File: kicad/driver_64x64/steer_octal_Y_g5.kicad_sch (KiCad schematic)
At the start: 66 parts

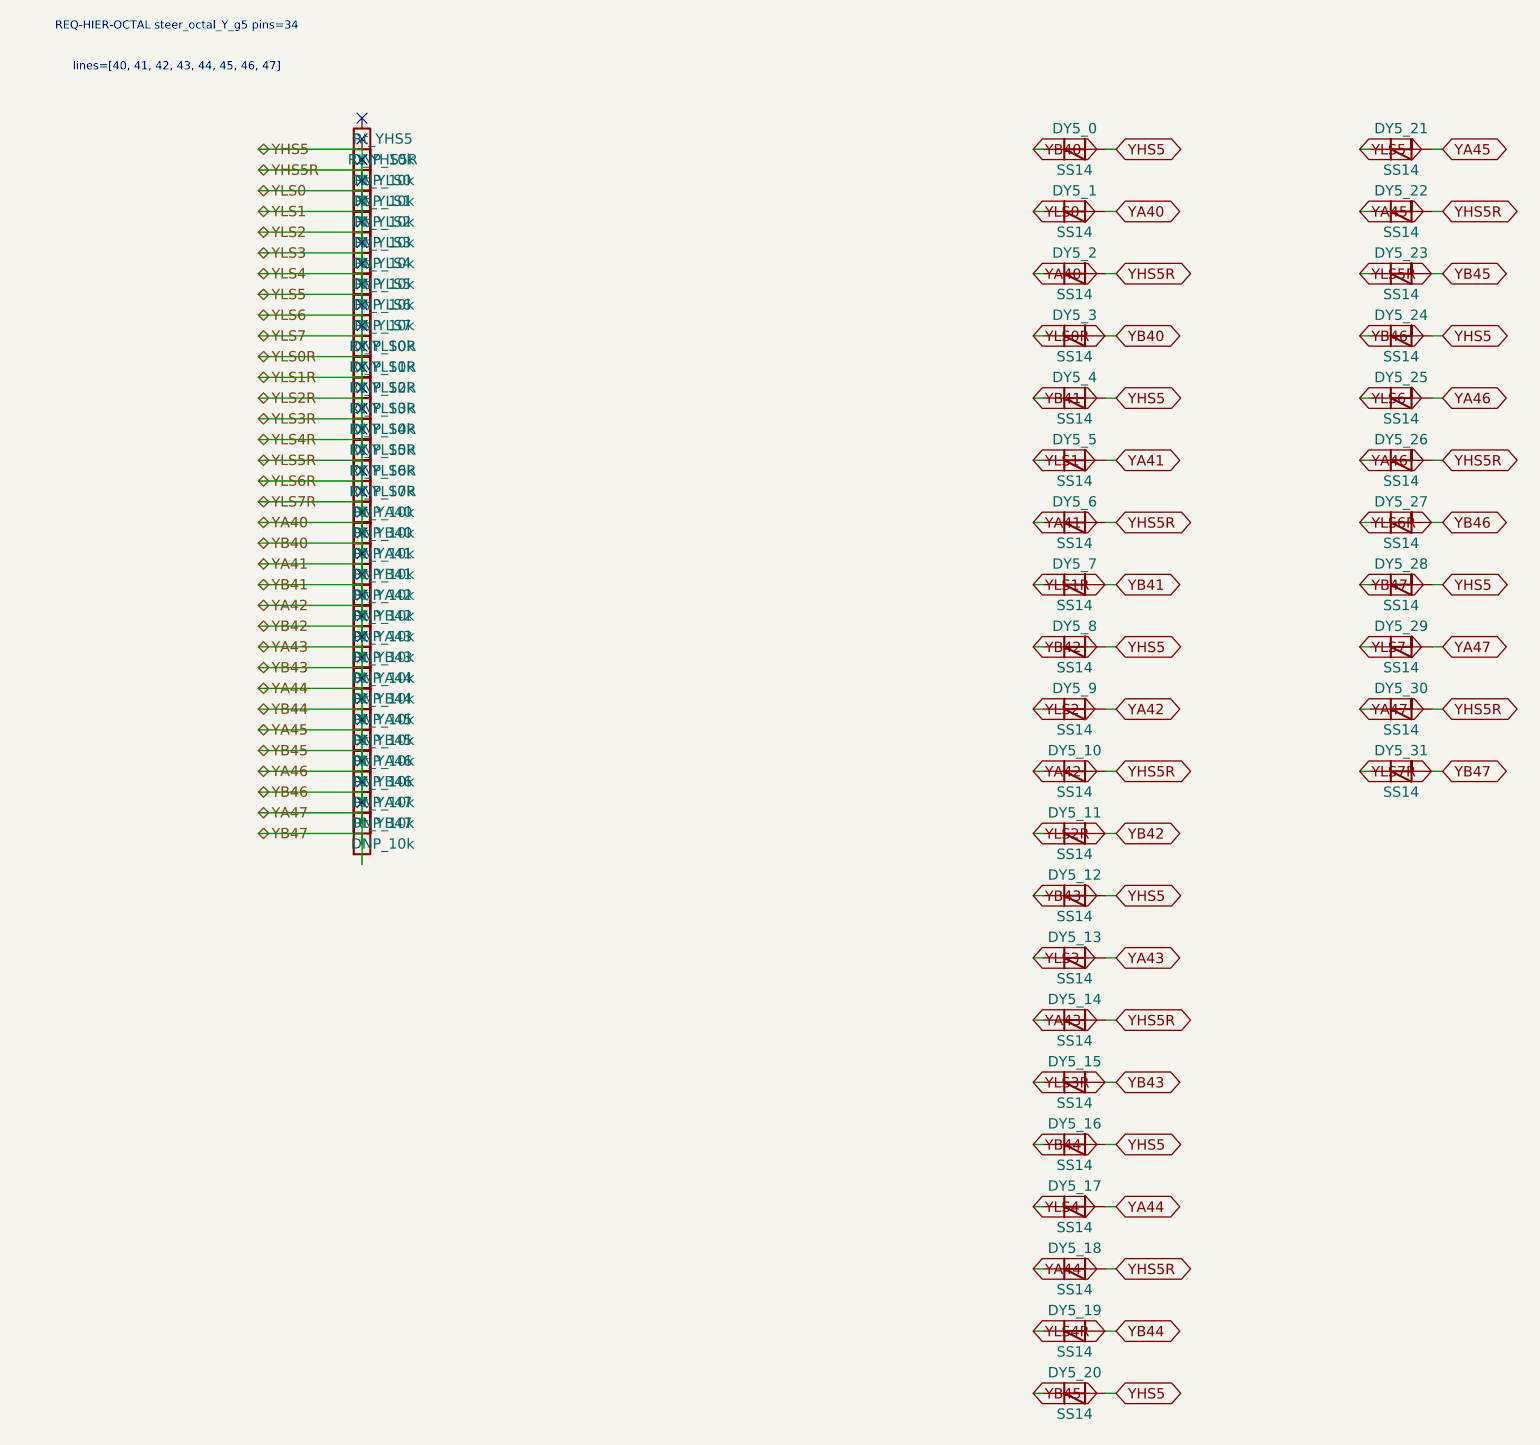
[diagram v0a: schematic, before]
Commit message: logical seperation into host and multiple decode/drive/steering boards
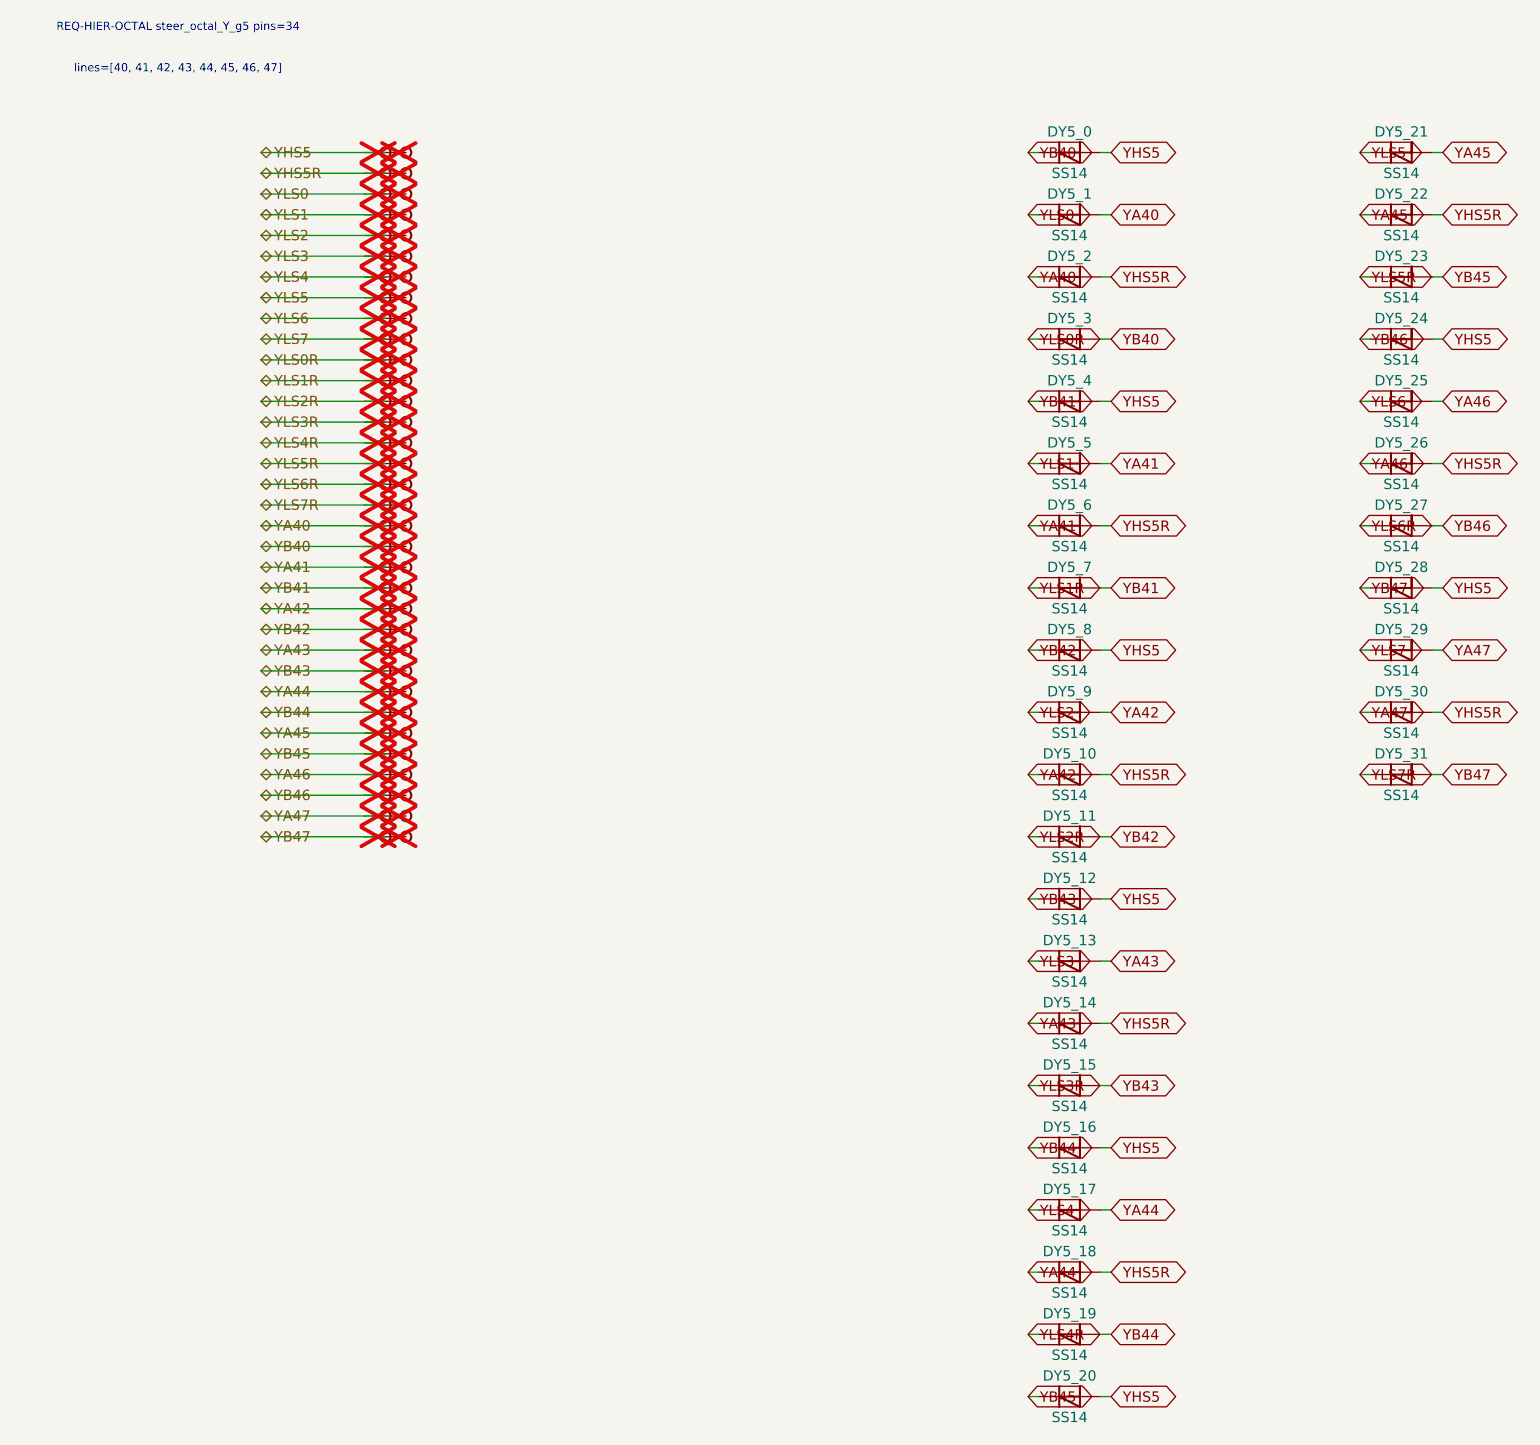
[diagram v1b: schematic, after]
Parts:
- removed Rt_YA40, Rt_YA41, Rt_YA42, Rt_YA43, Rt_YA44, Rt_YA45, Rt_YA46, Rt_YA47, Rt_YB40, Rt_YB41, Rt_YB42, Rt_YB43, Rt_YB44, Rt_YB45, Rt_YB46, Rt_YB47, Rt_YHS5, Rt_YHS5R, Rt_YLS0, Rt_YLS0R, Rt_YLS1, Rt_YLS1R, Rt_YLS2, Rt_YLS2R, Rt_YLS3, Rt_YLS3R, Rt_YLS4, Rt_YLS4R, Rt_YLS5, Rt_YLS5R, Rt_YLS6, Rt_YLS6R, Rt_YLS7, Rt_YLS7R: DNP_10k, symbol Device:R
- added TP_YA40, TP_YA40b, TP_YA41, TP_YA41b, TP_YA42, TP_YA42b, TP_YA43, TP_YA43b, TP_YA44, TP_YA44b, TP_YA45, TP_YA45b, TP_YA46, TP_YA46b, TP_YA47, TP_YA47b, TP_YB40, TP_YB40b, TP_YB41, TP_YB41b, TP_YB42, TP_YB42b, TP_YB43, TP_YB43b, TP_YB44, TP_YB44b, TP_YB45, TP_YB45b, TP_YB46, TP_YB46b, TP_YB47, TP_YB47b, TP_YHS5, TP_YHS5R, TP_YHS5Rb, TP_YHS5b, TP_YLS0, TP_YLS0R, TP_YLS0Rb, TP_YLS0b, TP_YLS1, TP_YLS1R, TP_YLS1Rb, TP_YLS1b, TP_YLS2, TP_YLS2R, TP_YLS2Rb, TP_YLS2b, TP_YLS3, TP_YLS3R, TP_YLS3Rb, TP_YLS3b, TP_YLS4, TP_YLS4R, TP_YLS4Rb, TP_YLS4b, TP_YLS5, TP_YLS5R, TP_YLS5Rb, TP_YLS5b, TP_YLS6, TP_YLS6R, TP_YLS6Rb, TP_YLS6b, TP_YLS7, TP_YLS7R, TP_YLS7Rb, TP_YLS7b: Stub, symbol CMR:Stub
- DY5_0, DY5_1, DY5_10, DY5_11, DY5_12, DY5_13, DY5_14, DY5_15, DY5_16, DY5_17, DY5_18, DY5_19, DY5_2, DY5_20, DY5_21, DY5_22, DY5_23, DY5_24, DY5_25, DY5_26, DY5_27, DY5_28, DY5_29, DY5_3, DY5_30, DY5_31, DY5_4, DY5_5, DY5_6, DY5_7, DY5_8, DY5_9: symbol Device:D_Schottky -> CMR:D_Schottky
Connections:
- net YA40: now also TP_YA40.1, TP_YA40b.1; no longer DY5_0.1 (K), DY5_0.2 (A), DY5_1.1 (K), DY5_10.1 (K), DY5_10.2 (A), DY5_11.1 (K), DY5_11.2 (A), DY5_12.1 (K), DY5_12.2 (A), DY5_13.1 (K), DY5_13.2 (A), DY5_14.1 (K), DY5_14.2 (A), DY5_15.1 (K), DY5_15.2 (A), DY5_16.1 (K), DY5_16.2 (A), DY5_17.1 (K), DY5_17.2 (A), DY5_18.1 (K), DY5_18.2 (A), DY5_19.1 (K), DY5_19.2 (A), DY5_2.2 (A), DY5_20.1 (K), DY5_20.2 (A), DY5_21.1 (K), DY5_21.2 (A), DY5_22.1 (K), DY5_22.2 (A), DY5_23.1 (K), DY5_23.2 (A), DY5_24.1 (K), DY5_24.2 (A), DY5_25.1 (K), DY5_25.2 (A), DY5_26.1 (K), DY5_26.2 (A), DY5_27.1 (K), DY5_27.2 (A), DY5_28.1 (K), DY5_28.2 (A), DY5_29.1 (K), DY5_29.2 (A), DY5_3.1 (K), DY5_3.2 (A), DY5_30.1 (K), DY5_30.2 (A), DY5_31.1 (K), DY5_31.2 (A), DY5_4.1 (K), DY5_4.2 (A), DY5_5.1 (K), DY5_5.2 (A), DY5_6.1 (K), DY5_6.2 (A), DY5_7.1 (K), DY5_7.2 (A), DY5_8.1 (K), DY5_8.2 (A), DY5_9.1 (K), DY5_9.2 (A)
- new net YA41: DY5_5.2 (A), DY5_6.1 (K), TP_YA41.1, TP_YA41b.1
- new net YA42: DY5_10.1 (K), DY5_9.2 (A), TP_YA42.1, TP_YA42b.1
- new net YA43: DY5_13.2 (A), DY5_14.1 (K), TP_YA43.1, TP_YA43b.1
- new net YA44: DY5_17.2 (A), DY5_18.1 (K), TP_YA44.1, TP_YA44b.1
- new net YA45: DY5_21.2 (A), DY5_22.1 (K), TP_YA45.1, TP_YA45b.1
- new net YA46: DY5_25.2 (A), DY5_26.1 (K), TP_YA46.1, TP_YA46b.1
- new net YA47: DY5_29.2 (A), DY5_30.1 (K), TP_YA47.1, TP_YA47b.1
- new net YB40: DY5_0.1 (K), DY5_3.2 (A), TP_YB40.1, TP_YB40b.1
- new net YB41: DY5_4.1 (K), DY5_7.2 (A), TP_YB41.1, TP_YB41b.1
- new net YB42: DY5_11.2 (A), DY5_8.1 (K), TP_YB42.1, TP_YB42b.1
- new net YB43: DY5_12.1 (K), DY5_15.2 (A), TP_YB43.1, TP_YB43b.1
- new net YB44: DY5_16.1 (K), DY5_19.2 (A), TP_YB44.1, TP_YB44b.1
- new net YB45: DY5_20.1 (K), DY5_23.2 (A), TP_YB45.1, TP_YB45b.1
- new net YB46: DY5_24.1 (K), DY5_27.2 (A), TP_YB46.1, TP_YB46b.1
- new net YB47: DY5_28.1 (K), DY5_31.2 (A), TP_YB47.1, TP_YB47b.1
- new net YHS5: DY5_0.2 (A), DY5_12.2 (A), DY5_16.2 (A), DY5_20.2 (A), DY5_24.2 (A), DY5_28.2 (A), DY5_4.2 (A), DY5_8.2 (A), TP_YHS5.1, TP_YHS5b.1
- new net YHS5R: DY5_10.2 (A), DY5_14.2 (A), DY5_18.2 (A), DY5_2.2 (A), DY5_22.2 (A), DY5_26.2 (A), DY5_30.2 (A), DY5_6.2 (A), TP_YHS5R.1, TP_YHS5Rb.1
- new net YLS0: DY5_1.1 (K), TP_YLS0.1, TP_YLS0b.1
- new net YLS0R: DY5_3.1 (K), TP_YLS0R.1, TP_YLS0Rb.1
- new net YLS1: DY5_5.1 (K), TP_YLS1.1, TP_YLS1b.1
- new net YLS1R: DY5_7.1 (K), TP_YLS1R.1, TP_YLS1Rb.1
- new net YLS2: DY5_9.1 (K), TP_YLS2.1, TP_YLS2b.1
- new net YLS2R: DY5_11.1 (K), TP_YLS2R.1, TP_YLS2Rb.1
- new net YLS3: DY5_13.1 (K), TP_YLS3.1, TP_YLS3b.1
- new net YLS3R: DY5_15.1 (K), TP_YLS3R.1, TP_YLS3Rb.1
- new net YLS4: DY5_17.1 (K), TP_YLS4.1, TP_YLS4b.1
- new net YLS4R: DY5_19.1 (K), TP_YLS4R.1, TP_YLS4Rb.1
- new net YLS5: DY5_21.1 (K), TP_YLS5.1, TP_YLS5b.1
- new net YLS5R: DY5_23.1 (K), TP_YLS5R.1, TP_YLS5Rb.1
- new net YLS6: DY5_25.1 (K), TP_YLS6.1, TP_YLS6b.1
- new net YLS6R: DY5_27.1 (K), TP_YLS6R.1, TP_YLS6Rb.1
- new net YLS7: DY5_29.1 (K), TP_YLS7.1, TP_YLS7b.1
- new net YLS7R: DY5_31.1 (K), TP_YLS7R.1, TP_YLS7Rb.1
- no-connect marks 34 -> 0
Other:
- moved on the sheet: DY5_0, DY5_1, DY5_10, DY5_11, DY5_12, DY5_13, DY5_14, DY5_15, DY5_16, DY5_17, DY5_18, DY5_19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
